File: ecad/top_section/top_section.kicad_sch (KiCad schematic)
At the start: 13 parts, among them J1 JST SH 6P, J2 JST SH 6P, U1 Attiny1617-M, U2 LP5864

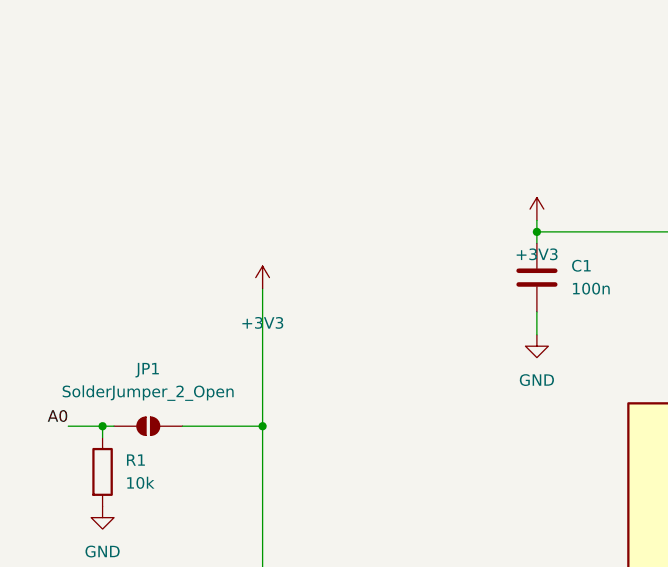
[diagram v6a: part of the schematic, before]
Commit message: Uses LED Matrix controller on all board.
It simplifies so much the design for a small cost.
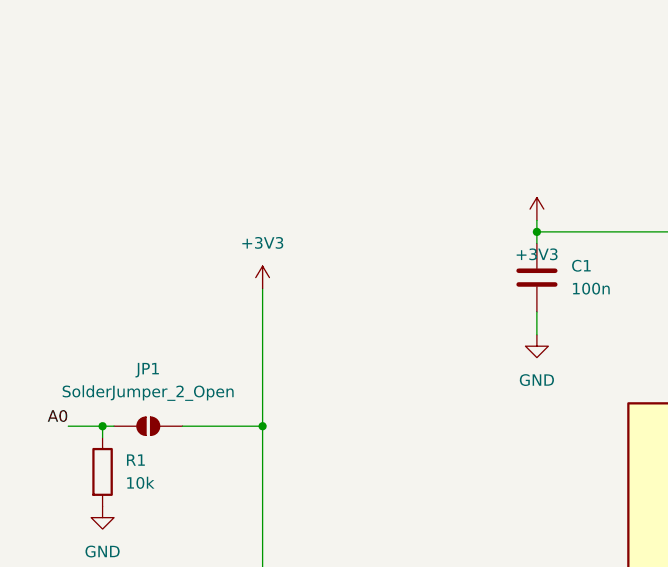
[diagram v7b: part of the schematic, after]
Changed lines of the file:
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@@
 		)
 		(property "Value" "+3V3"
-			(at 48.26 189.23 0)
+			(at 48.26 180.34 0)
 			(effects
 				(font

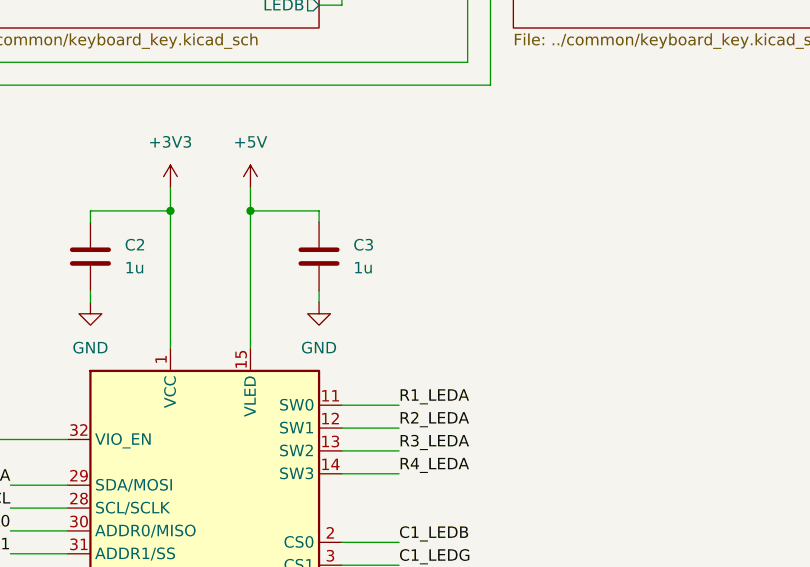
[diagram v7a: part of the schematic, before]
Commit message: Updated Controller for I2C controlled LED Matrices
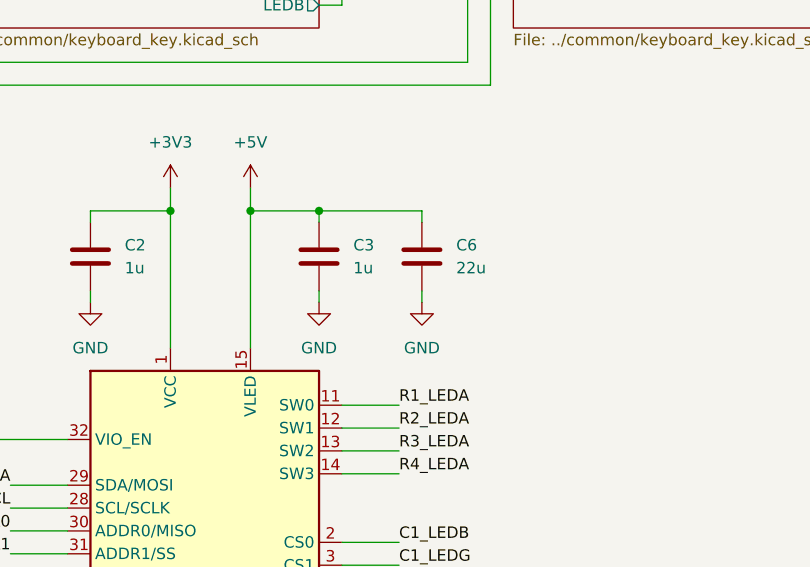
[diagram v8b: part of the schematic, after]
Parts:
- added C6: 22u, Capacitor_SMD:C_0805_2012Metric, symbol Device:C
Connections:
- net +5V: now also C6.1
- net GND: now also C6.2
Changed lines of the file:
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@@
 	)
 	(junction
+		(at 280.67 161.29)
+		(diameter 0)
+		(color 0 0 0 0)
+	)
+	(junction
 		(at 156.21 77.47)
 		(diameter 0)
@@
 	(wire
 		(pts
+			(xy 292.1 161.29) (xy 292.1 162.56)
+		)
+		(stroke
+			(width 0)
+			(type default)
+		)
+	)
+	(wire
+		(pts
 			(xy 217.17 97.79) (xy 227.33 97.79)
 		)
@@
 	(wire
 		(pts
+			(xy 292.1 170.18) (xy 292.1 171.45)
+		)
+		(stroke
+			(width 0)
+			(type default)
+		)
+	)
+	(wire
+		(pts
 			(xy 99.06 36.83) (xy 88.9 36.83)
 		)
@@
 	(wire
 		(pts
+			(xy 280.67 161.29) (xy 292.1 161.29)
+		)
+		(stroke
+			(width 0)
+			(type default)
+		)
+	)
+	(wire
+		(pts
 			(xy 175.26 100.33) (xy 170.18 100.33)
 		)
@@
 	(symbol
 		(lib_id "Device:C")
+		(at 292.1 166.37 0)
+		(unit 1)
+		(exclude_from_sim no)
+		(in_bom yes)
+		(on_board yes)
+		(dnp no)
+		(fields_autoplaced yes)
+		(property "Reference" "C6"
+			(at 295.91 165.0999 0)
+			(effects
+				(font
+					(size 1.27 1.27)
+				)
+				(justify left)
+			)
+		)
+		(property "Value" "22u"
+			(at 295.91 167.6399 0)
+			(effects
+				(font
+					(size 1.27 1.27)
+				)
+				(justify left)
+			)
+		)
+		(property "Footprint" "Capacitor_SMD:C_0805_2012Metric"
+			(at 293.0652 170.18 0)
+			(effects
+				(font
+					(size 1.27 1.27)
+				)
+				(hide yes)
+			)
+		)
+		(property "Datasheet" "~"
+			(at 292.1 166.37 0)
+			(effects
+				(font
+					(size 1.27 1.27)
+				)
+				(hide yes)
+			)
+		)
+		(property "Description" "Unpolarized capacitor"
+			(at 292.1 166.37 0)
+			(effects
+				(font
+					(size 1.27 1.27)
+				)
+				(hide yes)
+			)
+		)
+		(property "Manufacturer" ""
+			(at 292.1 166.37 0)
+			(effects
+				(font
+					(size 1.27 1.27)
+				)
+				(hide yes)
+			)
+		)
+		(pin "2"
+		)
+		(pin "1"
+		)
+		(instances
+			(project "top_section"
+				(path "/908c4fb0-9cf3-4739-9176-bc5c47ef8a7b"
+					(reference "C6")
+					(unit 1)
+				)
+			)
+		)
+	)
+	(symbol
+		(lib_id "Device:C")
 		(at 78.74 184.15 0)
 		(unit 1)
@@
 					(unit 1)
 				)
+			)
+		)
+	)
+	(symbol
+		(lib_id "power:GND")
+		(at 292.1 171.45 0)
+		(unit 1)
+		(exclude_from_sim no)
+		(in_bom yes)
+		(on_board yes)
+		(dnp no)
+		(fields_autoplaced yes)
+		(property "Reference" "#PWR022"
+			(at 292.1 177.8 0)
+			(effects
+				(font
+					(size 1.27 1.27)
+				)
+				(hide yes)
+			)
+		)
+		(property "Value" "GND"
+			(at 292.1 176.53 0)
+			(effects
+				(font
+					(size 1.27 1.27)
+				)
+			)
+		)
+		(property "Footprint" ""
+			(at 292.1 171.45 0)
+			(effects
+				(font
+					(size 1.27 1.27)
+				)
+				(hide yes)
+			)
+		)
+		(property "Datasheet" ""
+			(at 292.1 171.45 0)
+			(effects
+				(font
+					(size 1.27 1.27)
+				)
+				(hide yes)
+			)
+		)
+		(property "Description" "Power symbol creates a global label with name \"GND\" , ground"
+			(at 292.1 171.45 0)
+			(effects
+				(font
+					(size 1.27 1.27)
+				)
+				(hide yes)
+			)
+		)
+		(pin "1"
+		)
+		(instances
+			(project "top_section"
+				(path "/908c4fb0-9cf3-4739-9176-bc5c47ef8a7b"
+					(reference "#PWR022")
+					(unit 1)
+				)
